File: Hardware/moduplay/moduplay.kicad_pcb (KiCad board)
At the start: 2 copper layers, 72.2 x 91.5 mm, 16 parts, among them J2 -, J3 +, SW1 Left, SW10 Power, SW11 Buzzer, SW2 Up, SW3 Right, SW4 Down, SW5 X, SW6 Y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

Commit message: Add logo on PCBs
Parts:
- added REF**: Logo, carts:Logo, F.Cu at (178.8, 33.2)
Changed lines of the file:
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@@
 	(net 31 "Net-(J1-BUZZ1)")
 	(net 32 "Net-(J3-Pin_1)")
+	(footprint "carts:Logo"
+		(layer "F.Cu")
+		(at 178.75 33.25)
+		(property "Reference" "REF**"
+			(at 0 -5.08 0)
+			(unlocked yes)
+			(layer "F.SilkS")
+			(hide yes)
+			(effects
+				(font
+					(size 1 1)
+					(thickness 0.1)
+				)
+			)
+		)
+		(property "Value" "Logo"
+			(at 0 5.08 0)
+			(unlocked yes)
+			(layer "F.Fab")
+			(hide yes)
+			(effects
+				(font
+					(size 1 1)
+					(thickness 0.15)
+				)
+			)
+		)
+		(property "Datasheet" ""
+			(at 0 0 0)
+			(unlocked yes)
+			(layer "F.Fab")
+			(hide yes)
+			(effects
+				(font
+					(size 1 1)
+					(thickness 0.15)
+				)
+			)
+		)
+		(property "Description" ""
+			(at 0 0 0)
+			(unlocked yes)
+			(layer "F.Fab")
+			(hide yes)
+			(effects
+				(font
+					(size 1 1)
+					(thickness 0.15)
+				)
+			)
+		)
+		(attr smd)
+		(fp_line
+			(start -1 -2.75)
+			(end 0 -2.75)
+			(stroke
+				(width 1)
+				(type default)
+			)
+			(layer "F.SilkS")
+		)
+		(fp_line
+			(start -1 -0.25)
+			(end -1 0.5)
+			(stroke
+				(width 0.5)
+				(type default)
+			)
+			(layer "F.SilkS")
+		)
+		(fp_line
+			(start 1.5 1.25)
+			(end 1.5 -2.75)
+			(stroke
+				(width 1)
+				(type default)
+			)
+			(layer "F.SilkS")
+		)
+		(fp_line
+			(start 2 -0.75)
+			(end -0.5 -0.75)
+			(stroke
+				(width 0.5)
+				(type default)
+			)
+			(layer "F.SilkS")
+		)
+		(fp_line
+			(start 3.5 -2.75)
+			(end 1.5 -2.75)
+			(stroke
+				(width 1)
+				(type default)
+			)
+			(layer "F.SilkS")
+		)
+		(fp_line
+			(start 3.5 -0.75)
+			(end 1.5 -0.75)
+			(stroke
+				(width 1)
+				(type default)
+			)
+			(layer "F.SilkS")
+		)
+		(fp_line
+			(start 3.5 1.25)
+			(end 1.5 1.25)
+			(stroke
+				(width 1)
+				(type default)
+			)
+			(layer "F.SilkS")
+		)
+		(fp_line
+			(start 3.5 2.75)
+			(end -1 2.75)
+			(stroke
+				(width 1)
+				(type default)
+			)
+			(layer "F.SilkS")
+		)
+		(fp_arc
+			(start -1 2.75)
+			(mid -3.75 0)
+			(end -1 -2.75)
+			(stroke
+				(width 1)
+				(type default)
+			)
+			(layer "F.SilkS")
+		)
+		(fp_circle
+			(center -1 -0.75)
+			(end -0.5 -0.75)
+			(stroke
+				(width 0.5)
+				(type solid)
+			)
+			(fill no)
+			(layer "F.SilkS")
+		)
+		(fp_circle
+			(center -1 1)
+			(end -0.5 1)
+			(stroke
+				(width 0.5)
+				(type solid)
+			)
+			(fill no)
+			(layer "F.SilkS")
+		)
+		(fp_rect
+			(start -4.25 -3.25)
+			(end 4 3.25)
+			(stroke
+				(width 0.1)
+				(type solid)
+			)
+			(fill no)
+			(layer "F.CrtYd")
+		)
+		(fp_text user "${REFERENCE}"
+			(at -0.25 -4.25 0)
+			(unlocked yes)
+			(layer "F.Fab")
+			(effects
+				(font
+					(size 1 1)
+					(thickness 0.15)
+				)
+			)
+		)
+		(embedded_fonts no)
+	)
 	(footprint "Button_Switch_THT:SW_PUSH_6mm_H5mm"
 		(layer "F.Cu")

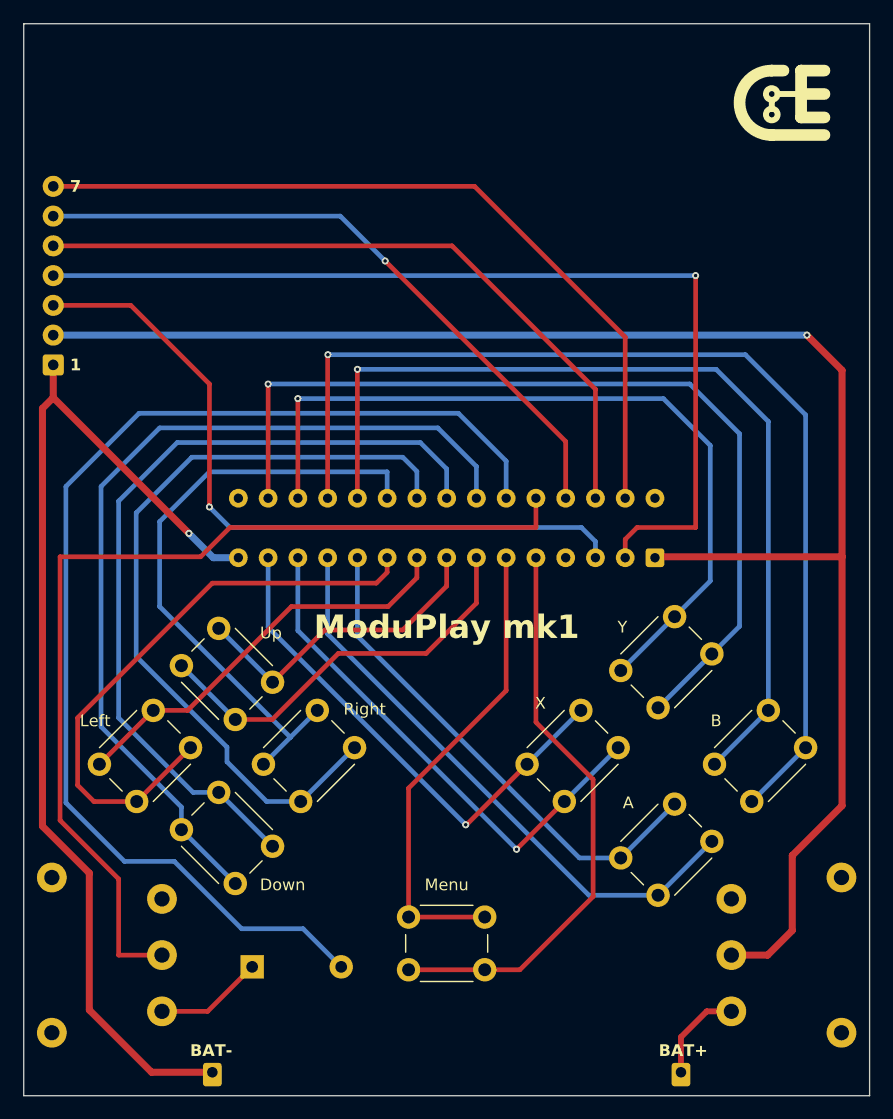
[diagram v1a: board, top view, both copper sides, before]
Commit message: Add holes to PCB
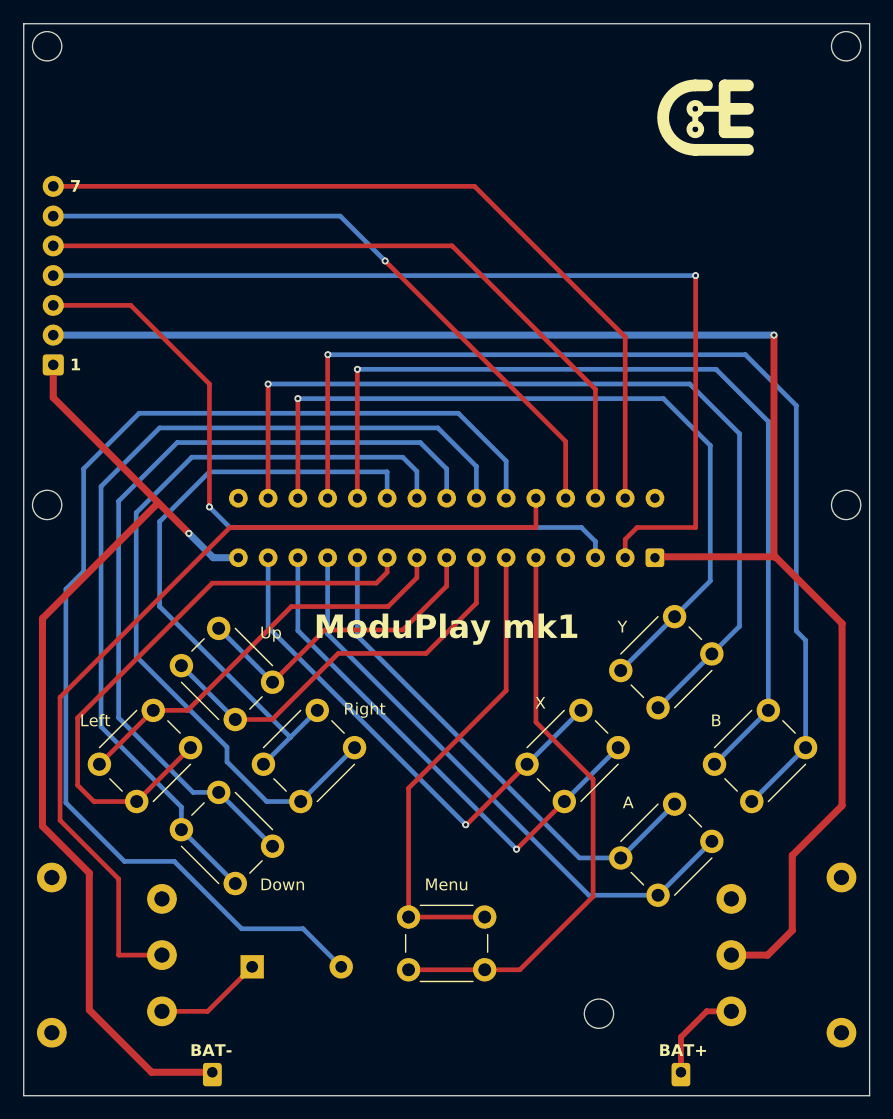
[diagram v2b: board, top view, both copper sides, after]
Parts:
- added REF**: MountingHole_2.5mm, MountingHole:MountingHole_2.5mm, F.Cu at (184.1, 28.4)
- added REF**: MountingHole_2.5mm, MountingHole:MountingHole_2.5mm, F.Cu at (163.0, 111.0)
- added REF**: MountingHole_2.5mm, MountingHole:MountingHole_2.5mm, F.Cu at (184.1, 67.6)
- added REF**: MountingHole_2.5mm, MountingHole:MountingHole_2.5mm, F.Cu at (115.9, 67.6)
- added REF**: MountingHole_2.5mm, MountingHole:MountingHole_2.5mm, F.Cu at (115.9, 28.4)
- moved REF** 6.65 mm to (172.2, 34.5)
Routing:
- net VCC: track 140.2 -> 132.9 mm
- net Net-(J1-BUZZ1): track 83.9 -> 76.9 mm
- net GND: track 91.3 -> 86.0 mm

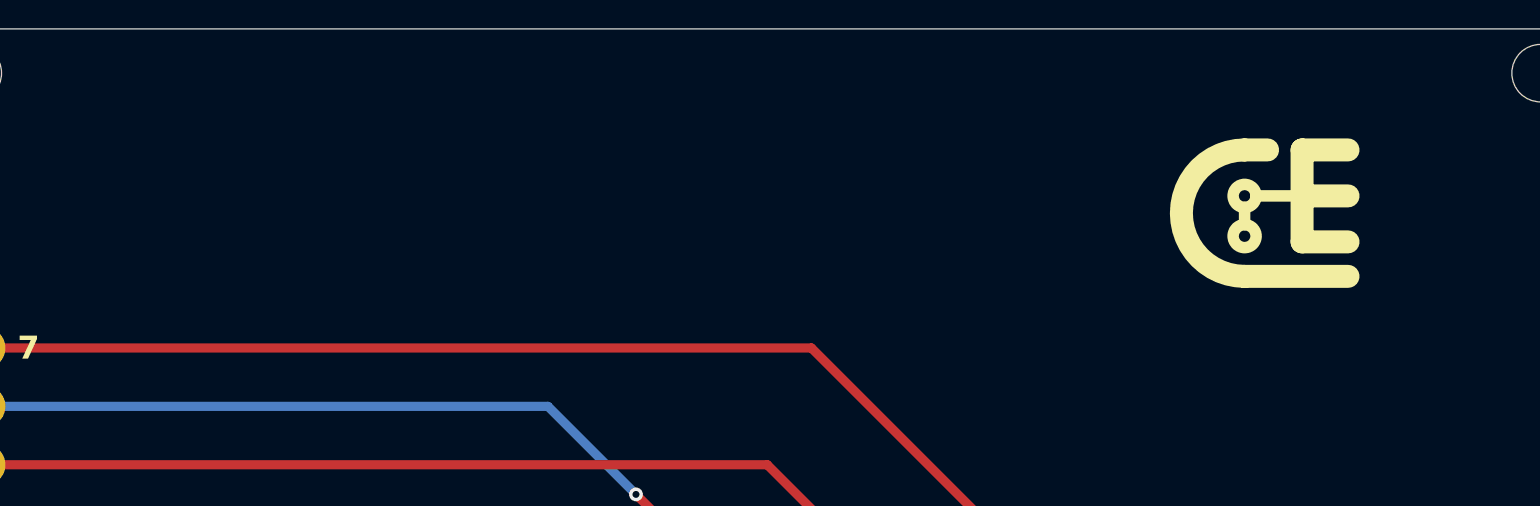
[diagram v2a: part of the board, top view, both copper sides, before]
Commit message: Fixes to comply to design rules
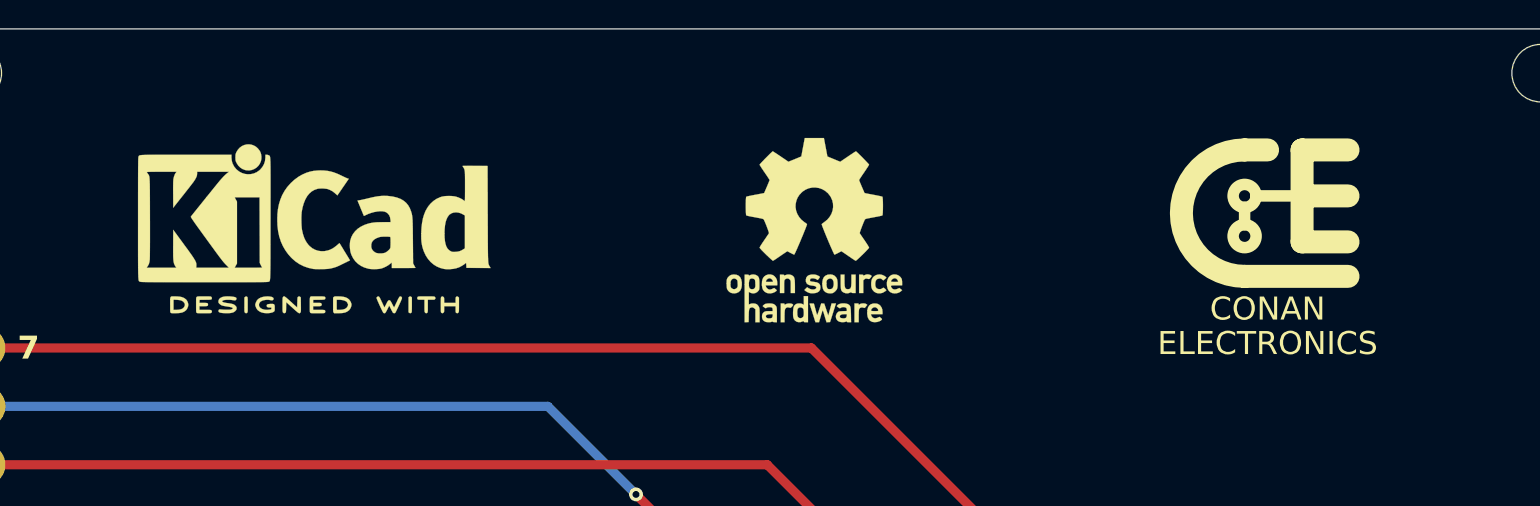
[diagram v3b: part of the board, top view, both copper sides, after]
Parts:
- added REF**: KiCad-Logo2_6mm_SilkScreen, Symbol:KiCad-Logo2_6mm_SilkScreen, F.Cu at (130.8, 34.5)
- added REF**: OSHW-Logo_7.5x8mm_SilkScreen, Symbol:OSHW-Logo_7.5x8mm_SilkScreen, F.Cu at (152.5, 35.2)
- REF**: value Logo -> Logo_Text; footprint carts:Logo -> carts:Logo_Text

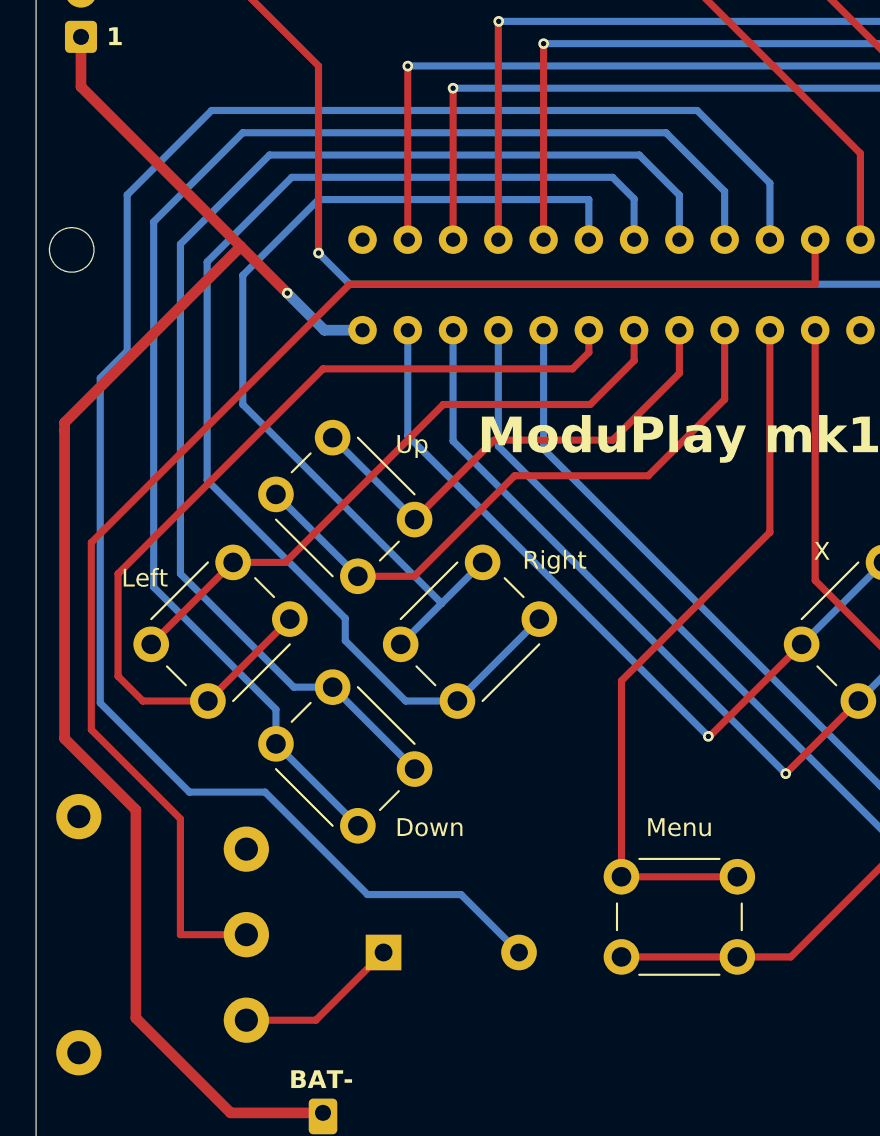
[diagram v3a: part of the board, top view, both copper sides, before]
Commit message: Fix buzzer connection
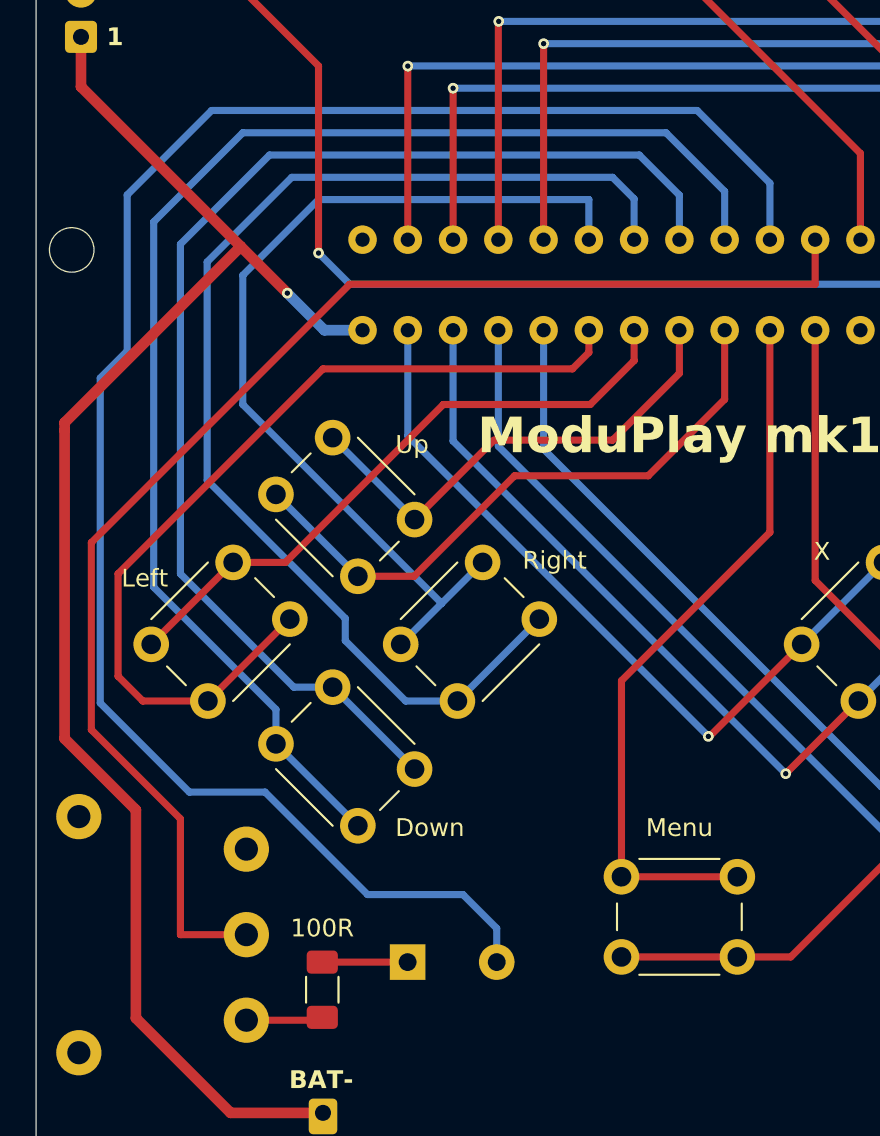
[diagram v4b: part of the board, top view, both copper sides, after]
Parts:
- added R1: 100R, Resistor_SMD:R_1206_3216Metric_Pad1.30x1.75mm_HandSolder, F.Cu at (130.0, 109.1)
- BZ1: footprint Buzzer_Beeper:Buzzer_12x9.5RM7.6 -> Buzzer_Beeper:Buzzer_TDK_PS1240P02BT_D12.2mm_H6.5mm
- DS1: value Display -> ~
- moved BZ1 1.45 mm to (134.8, 107.5)
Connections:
- SW11 pad 2: Net-(BZ1-+) -> Net-(R1-Pad1)
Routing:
- net Net-(BZ1-+): track 9.27 -> 4.79 mm
- net Net-(R1-Pad1): track 0.00 -> 4.33 mm
